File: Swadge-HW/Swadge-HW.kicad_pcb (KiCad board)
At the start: 2 copper layers, 136 x 75 mm, 90 parts, among them J1 SAO, J2 PJ-307C, J3 PGM, P1 USB_C_Plug_USB2.0, Q1 Q_PMOS_GSD, SW1 YTS-D003-1A, SW2 YTS-D003-1A, SW3 YTS-D003-1A, SW4 YTS-D003-1A, SW5 YTS-D003-1A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

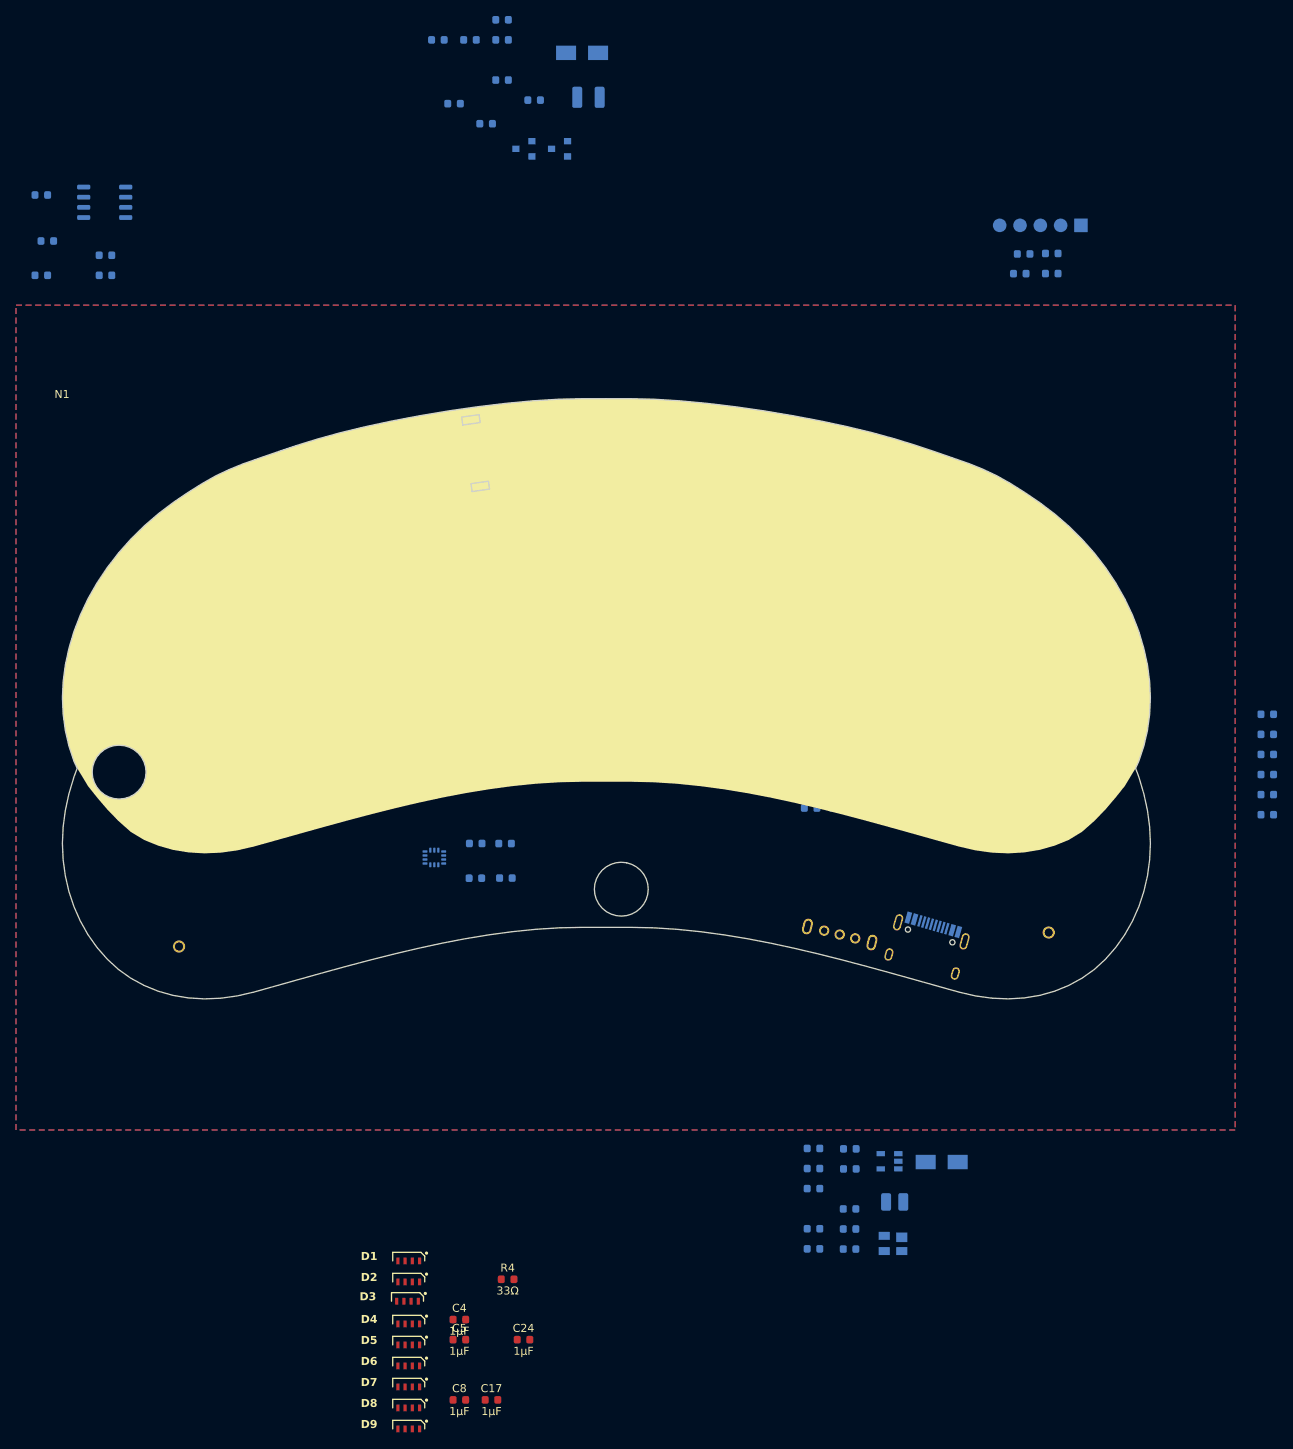
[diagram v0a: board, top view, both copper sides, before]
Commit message: Added condiment part
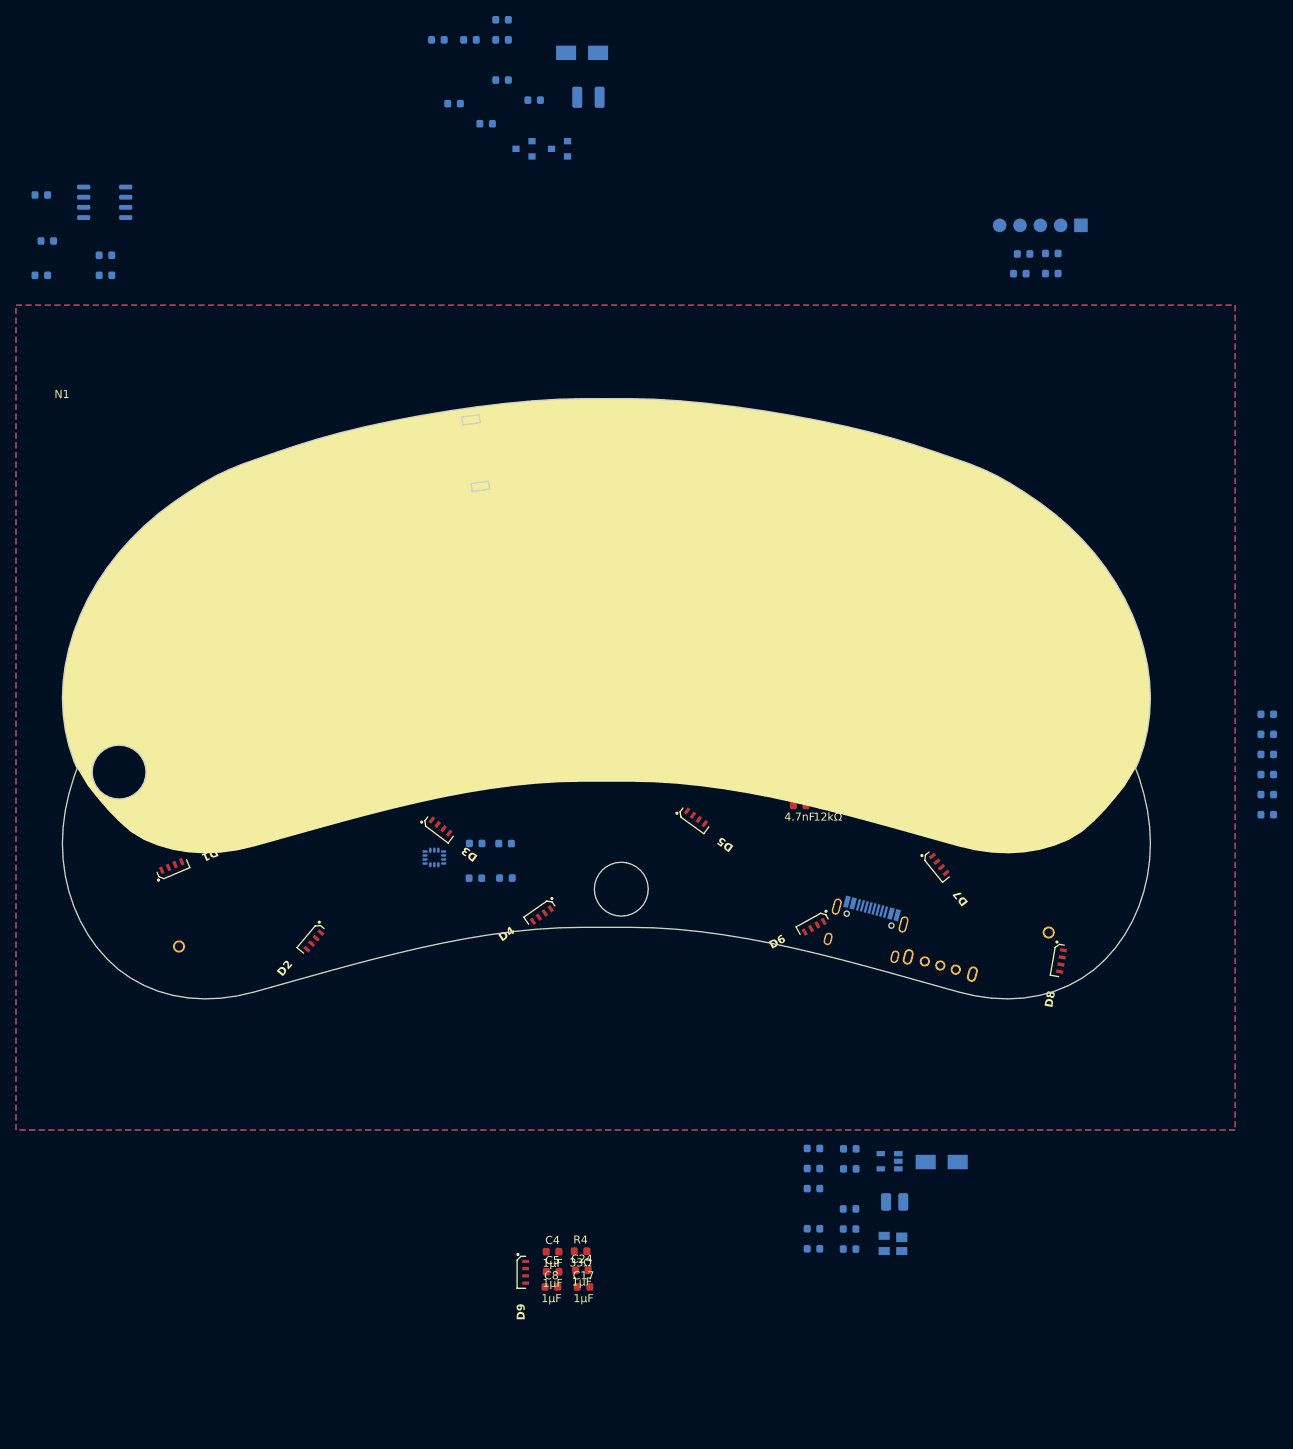
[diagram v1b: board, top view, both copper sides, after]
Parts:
- added N2: Condiment Acrylic, Swadge_Hotdog:condiment, F.Cu at (150.7, 124.2)
- C20, C9, R2, R3: moved to F.Cu
- moved D8 98.9 mm to (206.9, 132.8), turned to 80 degrees
- moved D7 93.1 mm to (191.6, 120.7), turned to 129 degrees
- moved D5 75.1 mm to (161.2, 114.8), turned to 144 degrees
- moved D6 74.7 mm to (176.0, 128.5), turned to 29 degrees
- moved D3 59.5 mm to (129.3, 116.0), turned to 143 degrees
- moved D1 57.6 mm to (95.7, 120.9), turned to -157 degrees
- moved D4 53.7 mm to (141.9, 127.0), turned to 35 degrees
- moved D2 44.3 mm to (113.4, 130.3), turned to 50 degrees
- moved D9 24.4 mm to (139.9, 171.7), turned to 90 degrees
- moved C17 18.2 mm to (147.1, 173.5)
- moved C8 18.2 mm to (143.1, 173.5)
- moved C4 14.4 mm to (143.3, 169.1)
- moved C5 14.4 mm to (143.3, 171.6)
- moved SW9 13.2 mm to (191.7, 133.3), turned to 165 degrees
- moved C24 11.3 mm to (146.9, 171.4)
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
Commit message: Layout v0.5
Placement of 80% of SMD components
Add QMC6309
DNP D9
Move Power Switch to right dog
Bump Aux port over
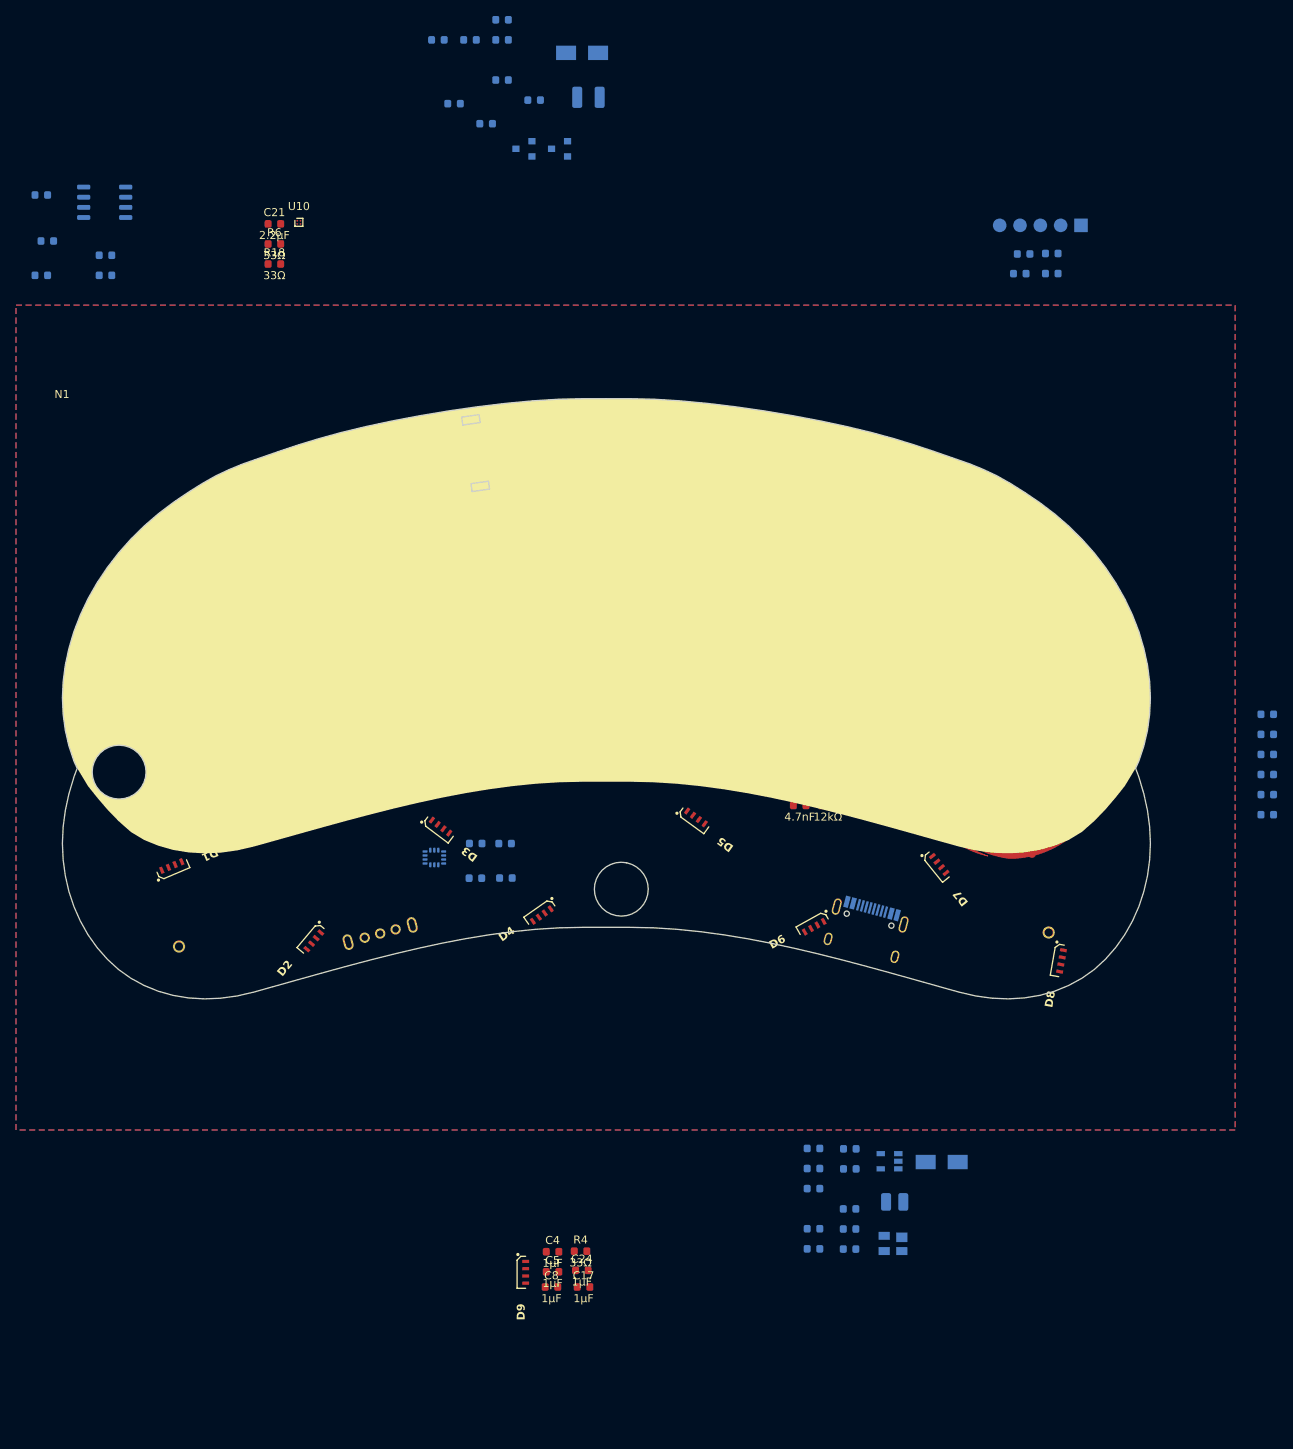
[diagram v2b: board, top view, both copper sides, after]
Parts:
- added C21: 2.2μF, Swadge_Parts:C_0603_1608Metric, F.Cu at (108.5, 40.6)
- added R18: 33Ω, Swadge_Parts:R_0603_1608Metric, F.Cu at (108.5, 45.7)
- added R6: 33Ω, Swadge_Parts:R_0603_1608Metric, F.Cu at (108.5, 43.1)
- added U10: ~, Swadge_Parts:BGA-4-.83x.83, F.Cu at (111.6, 40.4)
- moved SW9 70.1 mm to (121.7, 129.3), turned to -165 degrees
- moved U4 1.86 mm to (188.2, 95.6)
- moved SW7 1.54 mm to (186.2, 87.9)
- moved SW8 1.54 mm to (198.6, 83.4)

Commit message: Layout 0.6
still tweaking
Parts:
- removed C8: 1μF, Swadge_Parts:C_0603_1608Metric
- removed D9: LC8812B-4020, Swadge_Parts:4020PAD
- C11, C16, C19, C23, C25, R26, R7: moved to F.Cu
- C21, U10: moved to B.Cu
- R18, R6: value 33Ω -> 47kΩ; moved to B.Cu
- moved C18 74.7 mm to (144.3, 81.0), turned to 90 degrees
- moved U7 74.6 mm to (210.3, 55.3)
- moved C4 73.9 mm to (88.1, 119.9)
- moved R4 73.8 mm to (92.2, 119.4)
- moved R9 69.8 mm to (139.9, 81.8)
- moved C24 69.2 mm to (196.3, 122.9)
- moved C14 67.4 mm to (139.7, 87.1), turned to -90 degrees
- moved U8 67.4 mm to (133.2, 87.2)
- moved R5 66.7 mm to (128.3, 82.3), turned to 0 degrees
- moved C21 66.5 mm to (156.0, 87.1), turned to 90 degrees
- moved R6 64.3 mm to (152.1, 90.4), turned to 180 degrees
- moved D10 63.4 mm to (200.7, 52.8)
- moved C17 62.8 mm to (155.2, 111.3)
- moved U10 61.9 mm to (152.2, 87.2), turned to 180 degrees
- moved C22 61.9 mm to (185.6, 53.3)
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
